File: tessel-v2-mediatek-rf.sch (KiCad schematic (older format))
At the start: 43 parts, among them J501 CONN_01X01, J502 CONN_01X01, T501 2450BL15B100, T502 2450BL15B100, U201 MT7620N

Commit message: cross check with jia
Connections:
- net RF0_BALUN_IN_N: now also T501.4 (BAL); no longer T501.3 (BAL)
- net RF0_BALUN_IN_P: now also T501.3 (BAL); no longer T501.4 (BAL)
- net RF0_BALUN_OUT: no longer R507.2
- net RF1_BALUN_OUT: no longer R508.2
- net RF0_CHIP_ANT renamed RF0_FEED
- net RF0_FEED: now also R507.2
- net RF1_CHIP_ANT renamed RF1_FEED
- net RF1_FEED: now also R508.2
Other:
- moved on the sheet: R507, R508
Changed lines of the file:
@@
 L R R507
 U 1 1 549247BD
-P 11400 2750
-F 0 "R507" V 11480 2750 40  0000 C CNN
-F 1 "0R DNP" V 11407 2751 40  0000 C CNN
-F 2 "tm-kicad-lib:SMD-0402" V 11330 2750 30  0001 C CNN
-F 3 "" H 11400 2750 30  0000 C CNN
-	1    11400 2750
+P 11950 2750
+F 0 "R507" V 12030 2750 40  0000 C CNN
+F 1 "0R DNP" V 11957 2751 40  0000 C CNN
+F 2 "tm-kicad-lib:SMD-0402" V 11880 2750 30  0001 C CNN
+F 3 "" H 11950 2750 30  0000 C CNN
+	1    11950 2750
 	0    1    1    0
 $EndComp
@@
 Text Label 5200 4200 0    60   ~ 0
 RF0_OUTN
-Text Label 11900 2750 0    60   ~ 0
+Text Label 12200 2750 0    60   ~ 0
 RF0_UFL
-Text Label 10700 3550 1    60   ~ 0
+Text Label 10200 3750 0    60   ~ 0
 RF0_BALUN_OUT
 Text Label 11900 3750 0    60   ~ 0
-RF0_CHIP_ANT
+RF0_FEED
 Text Label 6900 3600 0    60   ~ 0
 RF0_OUTP_TCIN
@@
 L R R508
 U 1 1 5492F3FF
-P 11400 6600
-F 0 "R508" V 11480 6600 40  0000 C CNN
-F 1 "0R DNP" V 11407 6601 40  0000 C CNN
-F 2 "tm-kicad-lib:SMD-0402" V 11330 6600 30  0001 C CNN
-F 3 "" H 11400 6600 30  0000 C CNN
-	1    11400 6600
+P 12000 6600
+F 0 "R508" V 12080 6600 40  0000 C CNN
+F 1 "0R DNP" V 12007 6601 40  0000 C CNN
+F 2 "tm-kicad-lib:SMD-0402" V 11930 6600 30  0001 C CNN
+F 3 "" H 12000 6600 30  0000 C CNN
+	1    12000 6600
 	0    1    1    0
 $EndComp
@@
 Text Label 5200 8050 0    60   ~ 0
 RF1_OUTN
-Text Label 11900 6600 0    60   ~ 0
+Text Label 12250 6600 0    60   ~ 0
 RF1_UFL
-Text Label 10700 7400 1    60   ~ 0
+Text Label 10200 7600 0    60   ~ 0
 RF1_BALUN_OUT
 Text Label 11900 7600 0    60   ~ 0
-RF1_CHIP_ANT
+RF1_FEED
 Text Label 6900 7450 0    60   ~ 0
 RF1_OUTP_TCIN
@@
 Connection ~ 5900 3600
 Wire Wire Line
-	11150 2750 10700 2750
+	11700 2750 11600 2750
 Connection ~ 10700 3750
 Wire Wire Line
 	11500 3750 12700 3750
 Wire Wire Line
-	11650 2750 12600 2750
+	12200 2750 12600 2750
 Wire Wire Line
 	11800 7600 11800 8300
@@
 	5900 7350 5900 7450
 Connection ~ 5900 7450
-Wire Wire Line
-	11150 6600 10700 6600
 Connection ~ 10700 7600
 Wire Wire Line
 	11500 7600 12700 7600
 Wire Wire Line
-	11650 6600 12600 6600
+	12250 6600 12600 6600
 Wire Wire Line
 	2100 4550 2100 3600
@@
 	10200 3750 10900 3750
 Wire Wire Line
-	8100 3600 8900 3600
-Wire Wire Line
-	8900 3600 8900 3750
-Wire Wire Line
-	8100 4200 8900 4200
-Wire Wire Line
-	8900 4200 8900 4050
-Wire Wire Line
-	8900 3750 9000 3750
-Wire Wire Line
-	8900 4050 9000 4050
+	8100 3600 8950 3600
+Wire Wire Line
+	8900 4200 8100 4200
+Wire Wire Line
+	8900 3750 8900 4200
 $Comp
 L 2450BL15B100 T502
@@
 Text Label 8150 3600 0    60   ~ 0
 RF0_BALUN_IN_P
-Wire Wire Line
-	10700 2750 10700 3750
-Wire Wire Line
-	10700 6600 10700 7600
 Connection ~ 11800 8100
 Connection ~ 11800 4200
+Wire Wire Line
+	11600 2750 11600 3750
+Connection ~ 11600 3750
+Wire Wire Line
+	11750 6600 11650 6600
+Wire Wire Line
+	11650 6600 11650 7600
+Connection ~ 11650 7600
+Wire Wire Line
+	8900 3750 9000 3750
+Wire Wire Line
+	9000 4050 8950 4050
+Wire Wire Line
+	8950 4050 8950 3600
 $EndSCHEMATC

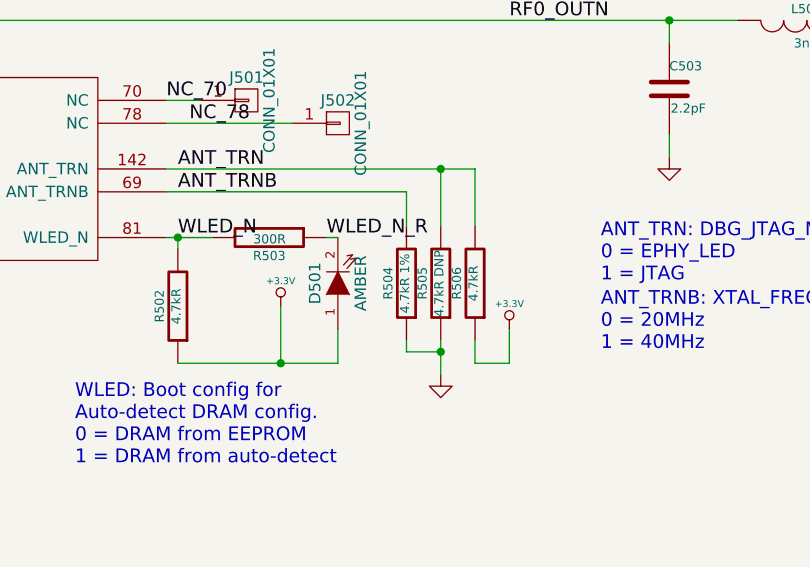
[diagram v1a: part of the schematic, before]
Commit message: usb lines routed
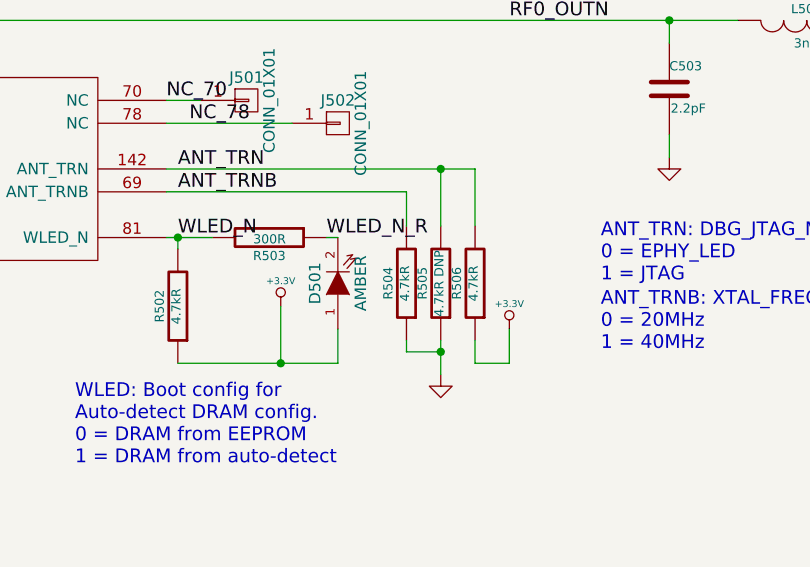
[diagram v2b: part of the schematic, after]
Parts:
- R504: value 4.7kR 1% -> 4.7kR
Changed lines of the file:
@@
 $EndComp
 $Comp
-L GND #PWR031
+L GND #PWR029
 U 1 1 5492119C
 P 10600 4350
-F 0 "#PWR031" H 10600 4350 30  0001 C CNN
+F 0 "#PWR029" H 10600 4350 30  0001 C CNN
 F 1 "GND" H 10600 4280 30  0001 C CNN
 F 2 "" H 10600 4350 60  0000 C CNN
@@
 $EndComp
 $Comp
-L GND #PWR032
+L GND #PWR030
 U 1 1 549211F2
 P 11800 4900
-F 0 "#PWR032" H 11800 4900 30  0001 C CNN
+F 0 "#PWR030" H 11800 4900 30  0001 C CNN
 F 1 "GND" H 11800 4830 30  0001 C CNN
 F 2 "" H 11800 4900 60  0000 C CNN
@@
 $EndComp
 $Comp
-L GND #PWR033
+L GND #PWR031
 U 1 1 54921339
 P 13100 3150
-F 0 "#PWR033" H 13100 3150 30  0001 C CNN
+F 0 "#PWR031" H 13100 3150 30  0001 C CNN
 F 1 "GND" H 13100 3080 30  0001 C CNN
 F 2 "" H 13100 3150 60  0000 C CNN
@@
 $EndComp
 $Comp
-L GND #PWR034
+L GND #PWR032
 U 1 1 54921B0A
 P 5900 4800
-F 0 "#PWR034" H 5900 4800 30  0001 C CNN
+F 0 "#PWR032" H 5900 4800 30  0001 C CNN
 F 1 "GND" H 5900 4730 30  0001 C CNN
 F 2 "" H 5900 4800 60  0000 C CNN
@@
 $EndComp
 $Comp
-L GND #PWR035
+L GND #PWR033
 U 1 1 54921B48
 P 5900 3000
-F 0 "#PWR035" H 5900 3000 30  0001 C CNN
+F 0 "#PWR033" H 5900 3000 30  0001 C CNN
 F 1 "GND" H 5900 2930 30  0001 C CNN
 F 2 "" H 5900 3000 60  0000 C CNN
@@
 $EndComp
 $Comp
-L GND #PWR036
+L GND #PWR034
 U 1 1 5492F3B9
 P 10600 8200
-F 0 "#PWR036" H 10600 8200 30  0001 C CNN
+F 0 "#PWR034" H 10600 8200 30  0001 C CNN
 F 1 "GND" H 10600 8130 30  0001 C CNN
 F 2 "" H 10600 8200 60  0000 C CNN
@@
 $EndComp
 $Comp
-L GND #PWR037
+L GND #PWR035
 U 1 1 5492F3BF
 P 11800 8800
-F 0 "#PWR037" H 11800 8800 30  0001 C CNN
+F 0 "#PWR035" H 11800 8800 30  0001 C CNN
 F 1 "GND" H 11800 8730 30  0001 C CNN
 F 2 "" H 11800 8800 60  0000 C CNN
@@
 $EndComp
 $Comp
-L GND #PWR038
+L GND #PWR036
 U 1 1 5492F3C5
 P 13100 7000
-F 0 "#PWR038" H 13100 7000 30  0001 C CNN
+F 0 "#PWR036" H 13100 7000 30  0001 C CNN
 F 1 "GND" H 13100 6930 30  0001 C CNN
 F 2 "" H 13100 7000 60  0000 C CNN
@@
 $EndComp
 $Comp
-L GND #PWR039
+L GND #PWR037
 U 1 1 5492F3D6
 P 5900 8650
-F 0 "#PWR039" H 5900 8650 30  0001 C CNN
+F 0 "#PWR037" H 5900 8650 30  0001 C CNN
 F 1 "GND" H 5900 8580 30  0001 C CNN
 F 2 "" H 5900 8650 60  0000 C CNN
@@
 $EndComp
 $Comp
-L GND #PWR040
+L GND #PWR038
 U 1 1 5492F3DC
 P 5900 6800
-F 0 "#PWR040" H 5900 6800 30  0001 C CNN
+F 0 "#PWR038" H 5900 6800 30  0001 C CNN
 F 1 "GND" H 5900 6730 30  0001 C CNN
 F 2 "" H 5900 6800 60  0000 C CNN
@@
 $EndComp
 $Comp
-L +3.3V #PWR041
+L +3.3V #PWR039
 U 1 1 54916FFB
 P 4200 5450
-F 0 "#PWR041" H 4200 5410 30  0001 C CNN
+F 0 "#PWR039" H 4200 5410 30  0001 C CNN
 F 1 "+3.3V" H 4200 5560 30  0000 C CNN
 F 2 "" H 4200 5450 60  0000 C CNN
@@
 $EndComp
 $Comp
-L GND #PWR042
+L GND #PWR040
 U 1 1 54917BEF
 P 2050 5950
-F 0 "#PWR042" H 2050 5950 30  0001 C CNN
+F 0 "#PWR040" H 2050 5950 30  0001 C CNN
 F 1 "GND" H 2050 5880 30  0001 C CNN
 F 2 "" H 2050 5950 60  0000 C CNN
@@
 NC_78
 $Comp
-L GND #PWR043
+L GND #PWR041
 U 1 1 54918F7B
 P 4900 5750
-F 0 "#PWR043" H 4900 5750 30  0001 C CNN
+F 0 "#PWR041" H 4900 5750 30  0001 C CNN
 F 1 "GND" H 4900 5680 30  0001 C CNN
 F 2 "" H 4900 5750 60  0000 C CNN
@@
 $EndComp
 $Comp
-L +3.3V #PWR044
+L +3.3V #PWR042
 U 1 1 54919282
 P 5200 5550
-F 0 "#PWR044" H 5200 5510 30  0001 C CNN
+F 0 "#PWR042" H 5200 5510 30  0001 C CNN
 F 1 "+3.3V" H 5200 5660 30  0000 C CNN
 F 2 "" H 5200 5550 60  0000 C CNN
@@
 P 4750 5350
 F 0 "R504" V 4830 5350 40  0000 C CNN
-F 1 "4.7kR 1%" V 4757 5351 40  0000 C CNN
+F 1 "4.7kR" V 4757 5351 40  0000 C CNN
 F 2 "tm-kicad-lib:SMD-0402" V 4680 5350 30  0001 C CNN
 F 3 "" H 4750 5350 30  0000 C CNN
@@
 	10300 7900 10300 8200
 $Comp
-L GND #PWR045
+L GND #PWR043
 U 1 1 54BF867B
 P 10300 8200
-F 0 "#PWR045" H 10300 8200 30  0001 C CNN
+F 0 "#PWR043" H 10300 8200 30  0001 C CNN
 F 1 "GND" H 10300 8130 30  0001 C CNN
 F 2 "" H 10300 8200 60  0000 C CNN
@@
 	9500 8500 9500 8400
 $Comp
-L GND #PWR046
+L GND #PWR044
 U 1 1 54BF87B3
 P 9500 8500
-F 0 "#PWR046" H 9500 8500 30  0001 C CNN
+F 0 "#PWR044" H 9500 8500 30  0001 C CNN
 F 1 "GND" H 9500 8430 30  0001 C CNN
 F 2 "" H 9500 8500 60  0000 C CNN
@@
 	9500 4650 9500 4550
 $Comp
-L GND #PWR047
+L GND #PWR045
 U 1 1 54BF88AF
 P 9500 4650
-F 0 "#PWR047" H 9500 4650 30  0001 C CNN
+F 0 "#PWR045" H 9500 4650 30  0001 C CNN
 F 1 "GND" H 9500 4580 30  0001 C CNN
 F 2 "" H 9500 4650 60  0000 C CNN
@@
 	10300 4050 10300 4350
 $Comp
-L GND #PWR048
+L GND #PWR046
 U 1 1 54BF89CF
 P 10300 4350
-F 0 "#PWR048" H 10300 4350 30  0001 C CNN
+F 0 "#PWR046" H 10300 4350 30  0001 C CNN
 F 1 "GND" H 10300 4280 30  0001 C CNN
 F 2 "" H 10300 4350 60  0000 C CNN
@@
 $EndComp
 $Comp
-L GND #PWR049
+L GND #PWR047
 U 1 1 54BF1FF8
 P 13550 4300
-F 0 "#PWR049" H 13550 4300 30  0001 C CNN
+F 0 "#PWR047" H 13550 4300 30  0001 C CNN
 F 1 "GND" H 13550 4230 30  0001 C CNN
 F 2 "" H 13550 4300 60  0000 C CNN
@@
 $EndComp
 $Comp
-L GND #PWR050
+L GND #PWR048
 U 1 1 54BF258A
 P 13550 8200
-F 0 "#PWR050" H 13550 8200 30  0001 C CNN
+F 0 "#PWR048" H 13550 8200 30  0001 C CNN
 F 1 "GND" H 13550 8130 30  0001 C CNN
 F 2 "" H 13550 8200 60  0000 C CNN

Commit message: pushing for jia
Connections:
- net RF0_FEED: now also AE505.1; no longer AE501.1
- net RF1_FEED: now also AE506.1; no longer AE502.1
- net RF0_PCBA renamed RF0_CHANT
- net RF0_CHANT: now also AE501.1; no longer AE505.1
- net RF1_PCBA renamed RF1_CHANT
- net RF1_CHANT: now also AE502.1; no longer AE506.1
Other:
- moved on the sheet: AE501, AE502, AE505, AE506, R509, R510

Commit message: post-schematic review. changes in.
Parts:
- R502: value 4.7kR -> 100kR
- R503: value 300R -> 330R
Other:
- note added: "50 OHM DIFFERENTIAL"
- moved on the sheet: AE501, AE503, AE505, C502, C503, C504, C505, C506, C507, C508, C509, C510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

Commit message: added esd/gnd loop deterrent to sockets
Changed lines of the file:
@@
 $EndComp
 $Comp
-L GND #PWR037
+L GND #PWR035
 U 1 1 5492F3B9
 P 10600 8200
-F 0 "#PWR037" H 10600 8200 30  0001 C CNN
+F 0 "#PWR035" H 10600 8200 30  0001 C CNN
 F 1 "GND" H 10600 8130 30  0001 C CNN
 F 2 "" H 10600 8200 60  0000 C CNN
@@
 $EndComp
 $Comp
-L GND #PWR038
+L GND #PWR036
 U 1 1 5492F3BF
 P 11800 8800
-F 0 "#PWR038" H 11800 8800 30  0001 C CNN
+F 0 "#PWR036" H 11800 8800 30  0001 C CNN
 F 1 "GND" H 11800 8730 30  0001 C CNN
 F 2 "" H 11800 8800 60  0000 C CNN
@@
 $EndComp
 $Comp
-L GND #PWR039
+L GND #PWR037
 U 1 1 5492F3C5
 P 13100 7000
-F 0 "#PWR039" H 13100 7000 30  0001 C CNN
+F 0 "#PWR037" H 13100 7000 30  0001 C CNN
 F 1 "GND" H 13100 6930 30  0001 C CNN
 F 2 "" H 13100 7000 60  0000 C CNN
@@
 $EndComp
 $Comp
-L GND #PWR040
+L GND #PWR038
 U 1 1 5492F3D6
 P 5650 9250
-F 0 "#PWR040" H 5650 9250 30  0001 C CNN
+F 0 "#PWR038" H 5650 9250 30  0001 C CNN
 F 1 "GND" H 5650 9180 30  0001 C CNN
 F 2 "" H 5650 9250 60  0000 C CNN
@@
 $EndComp
 $Comp
-L GND #PWR041
+L GND #PWR039
 U 1 1 5492F3DC
 P 5650 8050
-F 0 "#PWR041" H 5650 8050 30  0001 C CNN
+F 0 "#PWR039" H 5650 8050 30  0001 C CNN
 F 1 "GND" H 5650 7980 30  0001 C CNN
 F 2 "" H 5650 8050 60  0000 C CNN
@@
 $EndComp
 $Comp
-L +3.3V #PWR042
+L +3.3V #PWR040
 U 1 1 54916FFB
 P 4200 5450
-F 0 "#PWR042" H 4200 5410 30  0001 C CNN
+F 0 "#PWR040" H 4200 5410 30  0001 C CNN
 F 1 "+3.3V" H 4200 5560 30  0000 C CNN
 F 2 "" H 4200 5450 60  0000 C CNN
@@
 $EndComp
 $Comp
-L GND #PWR043
+L GND #PWR041
 U 1 1 54917BEF
 P 2050 5950
-F 0 "#PWR043" H 2050 5950 30  0001 C CNN
+F 0 "#PWR041" H 2050 5950 30  0001 C CNN
 F 1 "GND" H 2050 5880 30  0001 C CNN
 F 2 "" H 2050 5950 60  0000 C CNN
@@
 NC_78
 $Comp
-L GND #PWR044
+L GND #PWR042
 U 1 1 54918F7B
 P 5150 5750
-F 0 "#PWR044" H 5150 5750 30  0001 C CNN
+F 0 "#PWR042" H 5150 5750 30  0001 C CNN
 F 1 "GND" H 5150 5680 30  0001 C CNN
 F 2 "" H 5150 5750 60  0000 C CNN
@@
 $EndComp
 $Comp
-L +3.3V #PWR045
+L +3.3V #PWR043
 U 1 1 54919282
 P 5450 5550
-F 0 "#PWR045" H 5450 5510 30  0001 C CNN
+F 0 "#PWR043" H 5450 5510 30  0001 C CNN
 F 1 "+3.3V" H 5450 5660 30  0000 C CNN
 F 2 "" H 5450 5550 60  0000 C CNN
@@
 $EndComp
 $Comp
-L GND #PWR046
+L GND #PWR044
 U 1 1 54BF867B
 P 10300 8200
-F 0 "#PWR046" H 10300 8200 30  0001 C CNN
+F 0 "#PWR044" H 10300 8200 30  0001 C CNN
 F 1 "GND" H 10300 8130 30  0001 C CNN
 F 2 "" H 10300 8200 60  0000 C CNN
@@
 $EndComp
 $Comp
-L GND #PWR047
+L GND #PWR045
 U 1 1 54BF87B3
 P 9500 8500
-F 0 "#PWR047" H 9500 8500 30  0001 C CNN
+F 0 "#PWR045" H 9500 8500 30  0001 C CNN
 F 1 "GND" H 9500 8430 30  0001 C CNN
 F 2 "" H 9500 8500 60  0000 C CNN
@@
 $EndComp
 $Comp
-L GND #PWR048
+L GND #PWR046
 U 1 1 54BF88AF
 P 9550 4200
-F 0 "#PWR048" H 9550 4200 30  0001 C CNN
+F 0 "#PWR046" H 9550 4200 30  0001 C CNN
 F 1 "GND" H 9550 4130 30  0001 C CNN
 F 2 "" H 9550 4200 60  0000 C CNN
@@
 $EndComp
 $Comp
-L GND #PWR049
+L GND #PWR047
 U 1 1 54BF89CF
 P 10350 3900
-F 0 "#PWR049" H 10350 3900 30  0001 C CNN
+F 0 "#PWR047" H 10350 3900 30  0001 C CNN
 F 1 "GND" H 10350 3830 30  0001 C CNN
 F 2 "" H 10350 3900 60  0000 C CNN
@@
 $EndComp
 $Comp
-L GND #PWR050
+L GND #PWR048
 U 1 1 54BF1FF8
 P 12950 3850
-F 0 "#PWR050" H 12950 3850 30  0001 C CNN
+F 0 "#PWR048" H 12950 3850 30  0001 C CNN
 F 1 "GND" H 12950 3780 30  0001 C CNN
 F 2 "" H 12950 3850 60  0000 C CNN
@@
 $EndComp
 $Comp
-L GND #PWR051
+L GND #PWR049
 U 1 1 54BF258A
 P 12650 8200
-F 0 "#PWR051" H 12650 8200 30  0001 C CNN
+F 0 "#PWR049" H 12650 8200 30  0001 C CNN
 F 1 "GND" H 12650 8130 30  0001 C CNN
 F 2 "" H 12650 8200 60  0000 C CNN
@@
 RF0_BALUN_IN_P
 Wire Wire Line
-	11850 3300 11850 3750
-Wire Wire Line
-	11850 3750 11850 3950
+	11850 3300 11850 3950
 Connection ~ 11850 3300
 Wire Wire Line
@@
 	7450 2650 6550 2650
 Wire Wire Line
-	1950 2650 5650 2650
-Wire Wire Line
-	5650 2650 5950 2650
+	1950 2650 5950 2650
 Connection ~ 5650 2650
 Wire Wire Line
-	2100 3600 5650 3600
-Wire Wire Line
-	5650 3600 5950 3600
+	2100 3600 5950 3600
 Wire Wire Line
 	6550 3600 7450 3600
@@
 	10650 3800 10650 3900
 Wire Wire Line
-	13150 2500 13150 2600
-Wire Wire Line
-	13150 2600 13150 2700
+	13150 2500 13150 2700
 Wire Wire Line
 	13150 2600 13050 2600
@@
 	11750 2300 11650 2300
 Wire Wire Line
-	11550 3300 11650 3300
-Wire Wire Line
-	11650 3300 11850 3300
-Wire Wire Line
-	11850 3300 12050 3300
+	11550 3300 12050 3300
 Wire Wire Line
 	12250 2300 12650 2300
 Wire Wire Line
-	11800 7600 11800 8100
-Wire Wire Line
-	11800 8100 11800 8300
+	11800 7600 11800 8300
 Connection ~ 11800 7600
 Wire Wire Line
@@
 	7450 8650 6550 8650
 Wire Wire Line
-	1900 8650 5650 8650
-Wire Wire Line
-	5650 8650 5950 8650
+	1900 8650 5950 8650
 Wire Wire Line
 	5650 8750 5650 8650
 Connection ~ 5650 8650
 Wire Wire Line
-	1800 7450 5650 7450
-Wire Wire Line
-	5650 7450 5950 7450
+	1800 7450 5950 7450
 Wire Wire Line
 	6550 7450 7450 7450
@@
 	10600 8100 10600 8200
 Wire Wire Line
-	13100 6800 13100 6900
-Wire Wire Line
-	13100 6900 13100 7000
+	13100 6800 13100 7000
 Wire Wire Line
 	13100 6900 13000 6900
@@
 Connection ~ 5650 7450
 Wire Wire Line
-	11500 7600 11650 7600
-Wire Wire Line
-	11650 7600 11800 7600
-Wire Wire Line
-	11800 7600 12000 7600
+	11500 7600 12000 7600
 Wire Wire Line
 	12250 6600 12600 6600
@@
 	4400 5150 4450 5150
 Wire Wire Line
-	3700 5150 3750 5150
-Wire Wire Line
-	3750 5150 3900 5150
+	3700 5150 3900 5150
 Wire Wire Line
 	4450 5700 4450 5550
 Wire Wire Line
-	2050 5150 2050 5200
-Wire Wire Line
-	2050 5200 2050 5250
+	2050 5150 2050 5250
 Wire Wire Line
 	2050 5150 2100 5150
 Wire Wire Line
-	2050 5750 2050 5850
-Wire Wire Line
-	2050 5850 2050 5950
+	2050 5750 2050 5950
 Wire Wire Line
 	2300 5300 2300 5200
@@
 	4200 5450 4200 5700
 Wire Wire Line
-	3750 5700 4200 5700
-Wire Wire Line
-	4200 5700 4450 5700
+	3750 5700 4450 5700
 Wire Wire Line
 	3700 4950 4750 4950
@@
 	4750 5650 4750 5600
 Wire Wire Line
-	5150 5600 5150 5650
-Wire Wire Line
-	5150 5650 5150 5750
+	5150 5600 5150 5750
 Connection ~ 5150 5650
 Wire Wire Line
@@
 Connection ~ 4200 5700
 Wire Wire Line
-	10250 3300 10650 3300
-Wire Wire Line
-	10650 3300 10950 3300
-Wire Wire Line
-	7850 3600 8150 3600
-Wire Wire Line
-	8150 3600 9050 3600
-Wire Wire Line
-	7850 2650 8150 2650
-Wire Wire Line
-	8150 2650 9000 2650
+	10250 3300 10950 3300
+Wire Wire Line
+	7850 3600 9050 3600
+Wire Wire Line
+	7850 2650 9000 2650
 Wire Wire Line
 	9000 2650 9000 3300
 Wire Wire Line
-	7850 7450 8150 7450
-Wire Wire Line
-	8150 7450 8900 7450
+	7850 7450 8900 7450
 Wire Wire Line
 	8900 7450 8900 7600
 Wire Wire Line
-	7850 8650 8150 8650
-Wire Wire Line
-	8150 8650 8900 8650
+	7850 8650 8900 8650
 Wire Wire Line
 	8900 8650 8900 7900
@@
 	8900 7900 9000 7900
 Wire Wire Line
-	10200 7600 10600 7600
-Wire Wire Line
-	10600 7600 10900 7600
+	10200 7600 10900 7600
 Wire Wire Line
 	10200 7900 10300 7900
@@
 	11800 8100 12200 8100
 Wire Wire Line
-	3700 4850 5150 4850
-Wire Wire Line
-	5150 4850 5300 4850
+	3700 4850 5300 4850
 Wire Wire Line
 	5300 4850 5300 5100
@@
 50 OHM DIFFERENTIAL
 $Comp
-L GND #PWR?
+L GND #PWR050
 U 1 1 54CA5F35
 P 5650 3250
-F 0 "#PWR?" H 5650 3250 30  0001 C CNN
+F 0 "#PWR050" H 5650 3250 30  0001 C CNN
 F 1 "GND" H 5650 3180 30  0001 C CNN
 F 2 "" H 5650 3250 60  0000 C CNN
@@
 	5650 3700 5650 3600
 $Comp
-L GND #PWR?
+L GND #PWR051
 U 1 1 54CA6384
 P 5650 4200
-F 0 "#PWR?" H 5650 4200 30  0001 C CNN
+F 0 "#PWR051" H 5650 4200 30  0001 C CNN
 F 1 "GND" H 5650 4130 30  0001 C CNN
 F 2 "" H 5650 4200 60  0000 C CNN

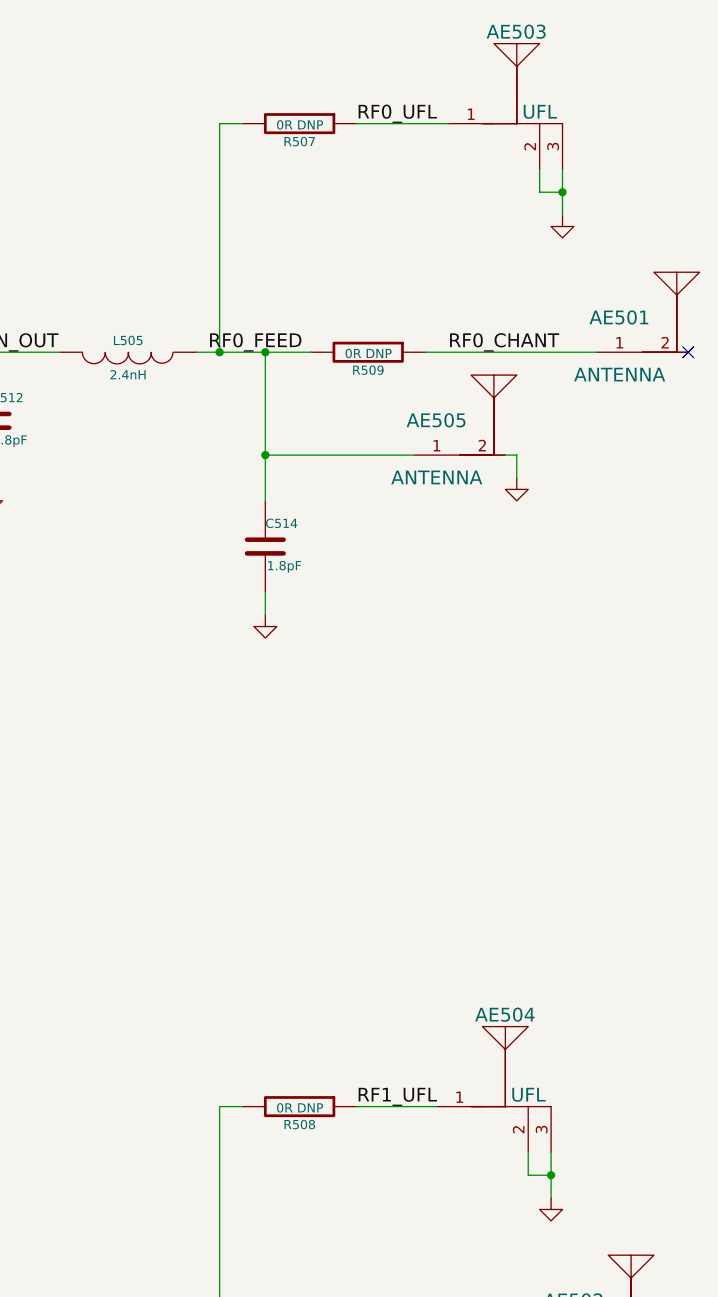
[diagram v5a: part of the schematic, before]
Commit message: rf power, removed 0R between RF_FEED and UFL
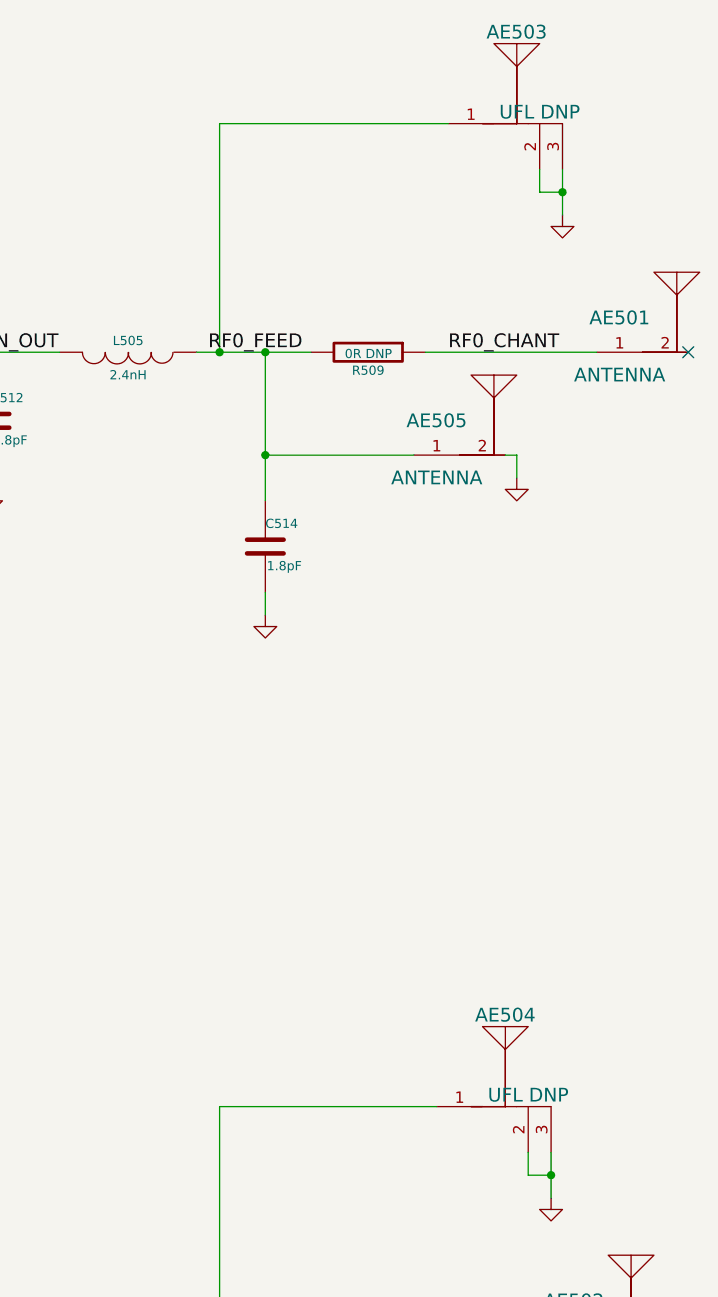
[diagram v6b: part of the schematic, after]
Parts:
- removed R507, R508: 0R DNP, tm-kicad-lib:SMD-0402, symbol R
- AE503, AE504: value UFL -> UFL DNP
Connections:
- net RF0_UFL is gone; now on net RF0_FEED: AE503.1
- net RF1_UFL is gone; now on net RF1_FEED: AE504.1
